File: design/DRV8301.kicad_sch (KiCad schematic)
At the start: 38 parts, among them U2 LM3671, U3 DRV8301

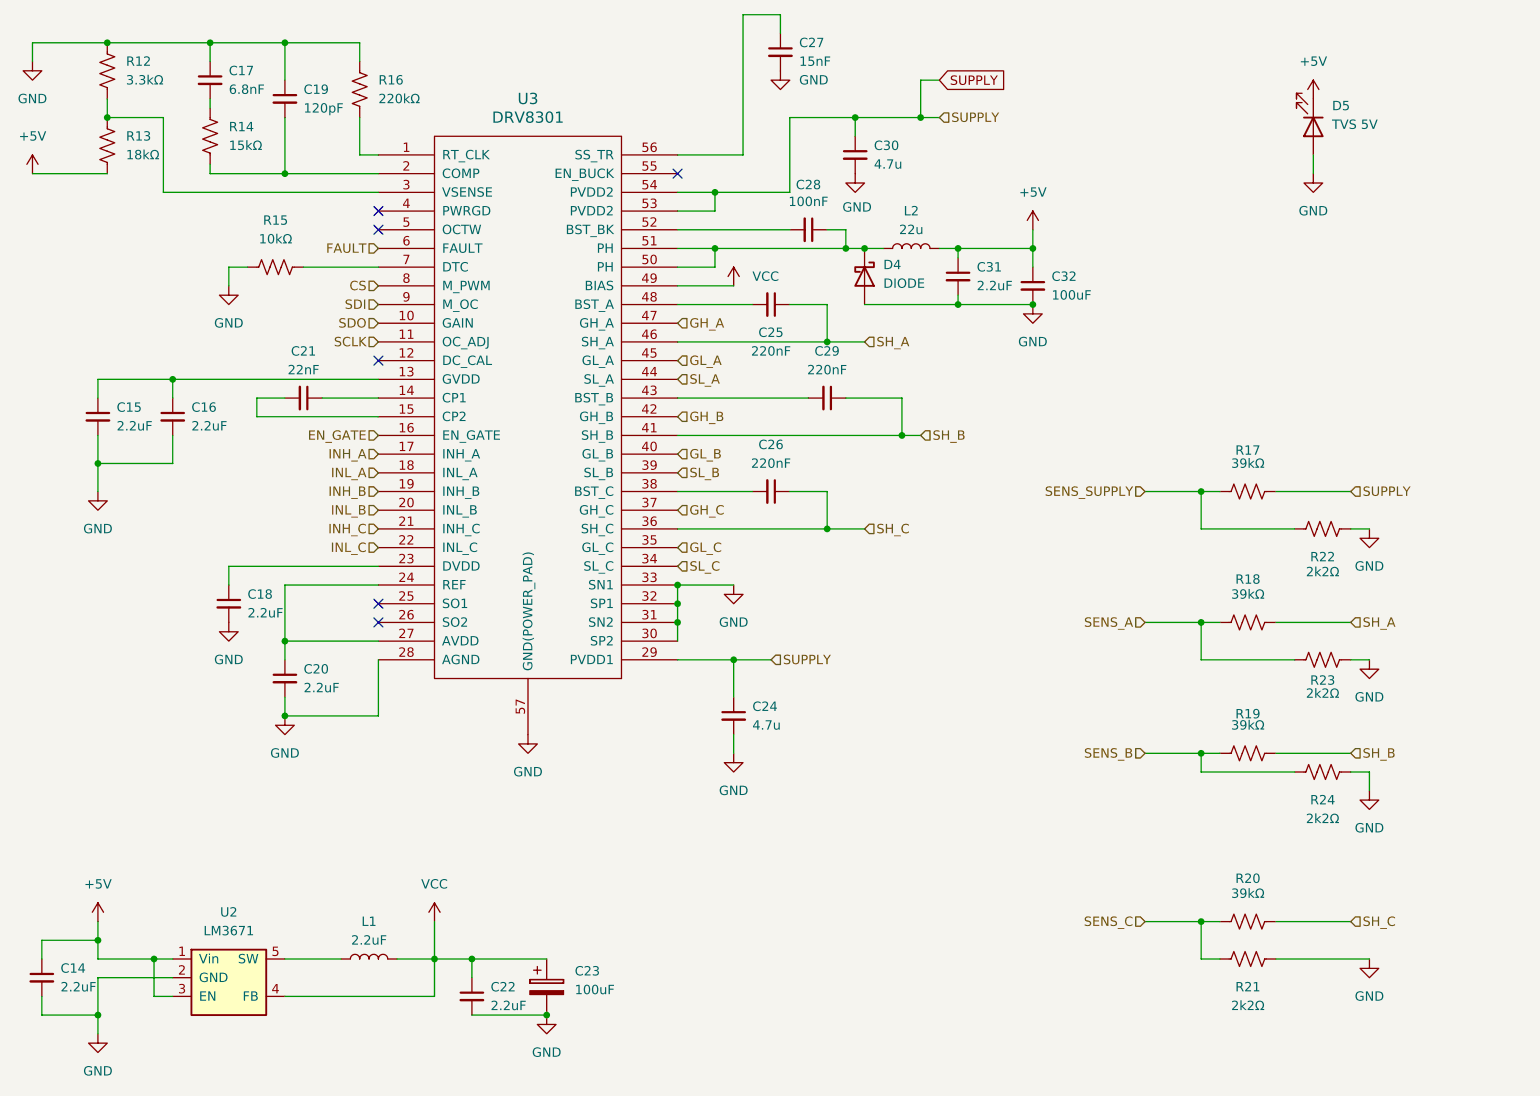
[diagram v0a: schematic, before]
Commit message: Agregado ibom
Pequeños cambios en el esquemático y agregado de ibom
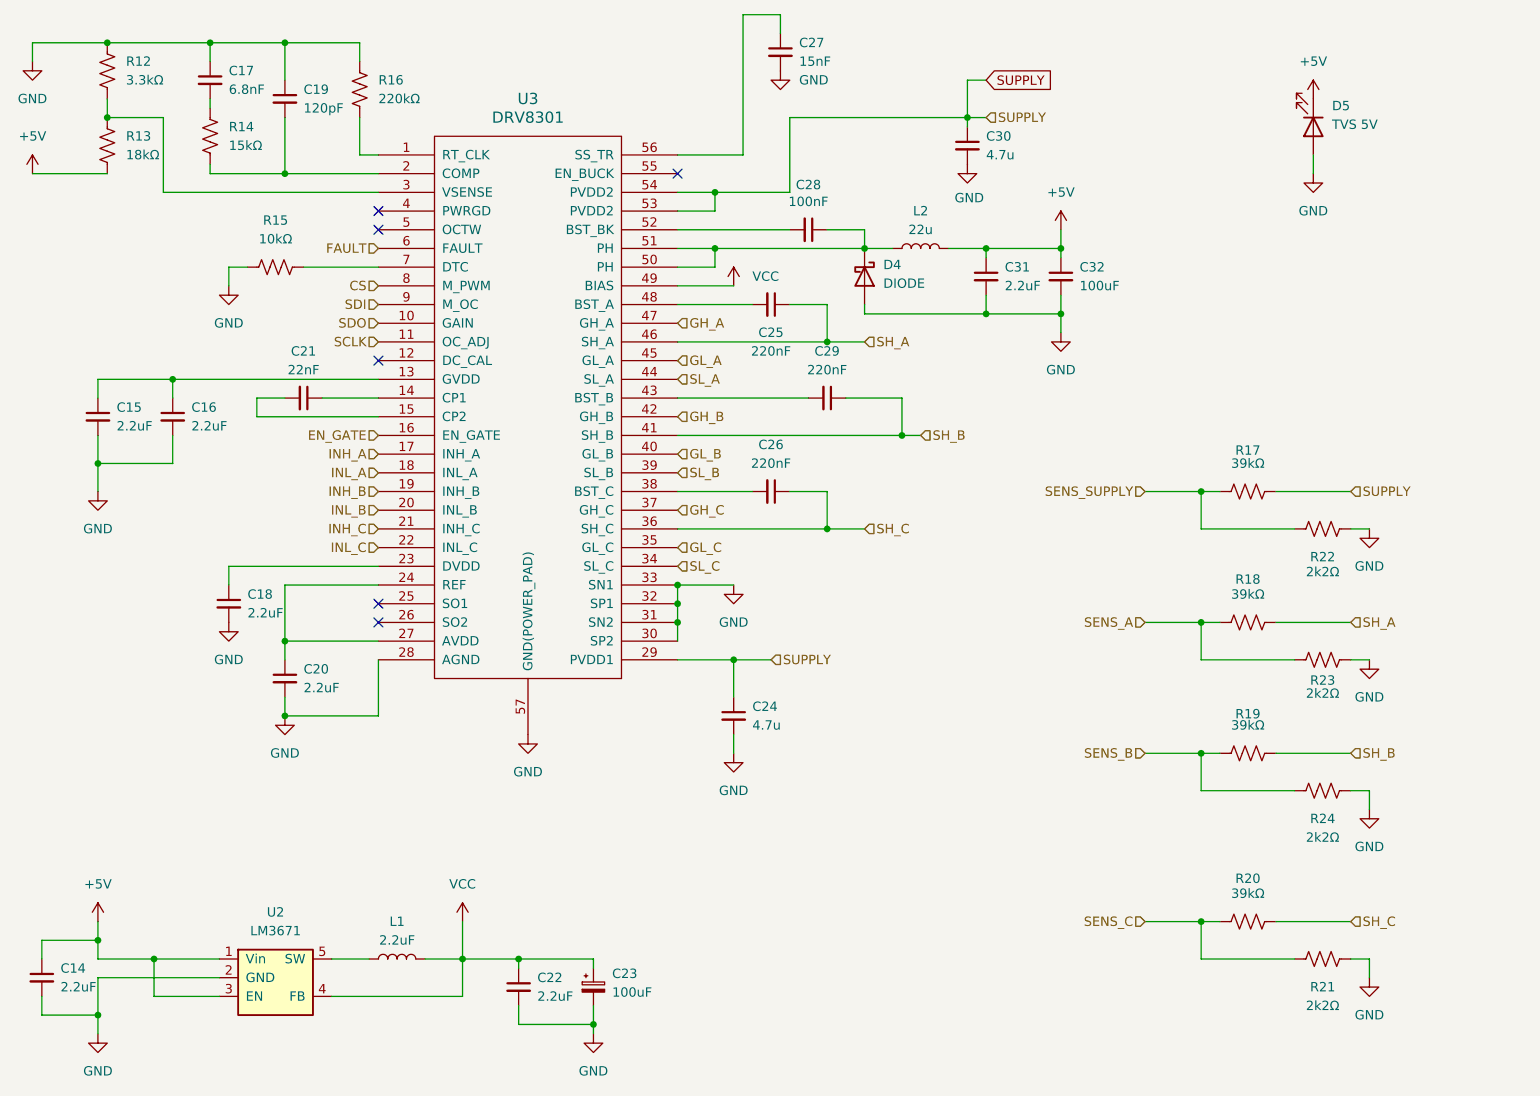
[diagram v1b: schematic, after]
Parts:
- C23: symbol ESCX-rescue:CP-Device -> Device:C_Polarized_Small
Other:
- moved on the sheet: C22, C30, C31, C32, L1, L2, R21, R24, U2

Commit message: Cambios en el esquemático
- Cambio de Vcc por +3.3V
- Agregado de hoja para desarrollar la entrada de tensión alterna
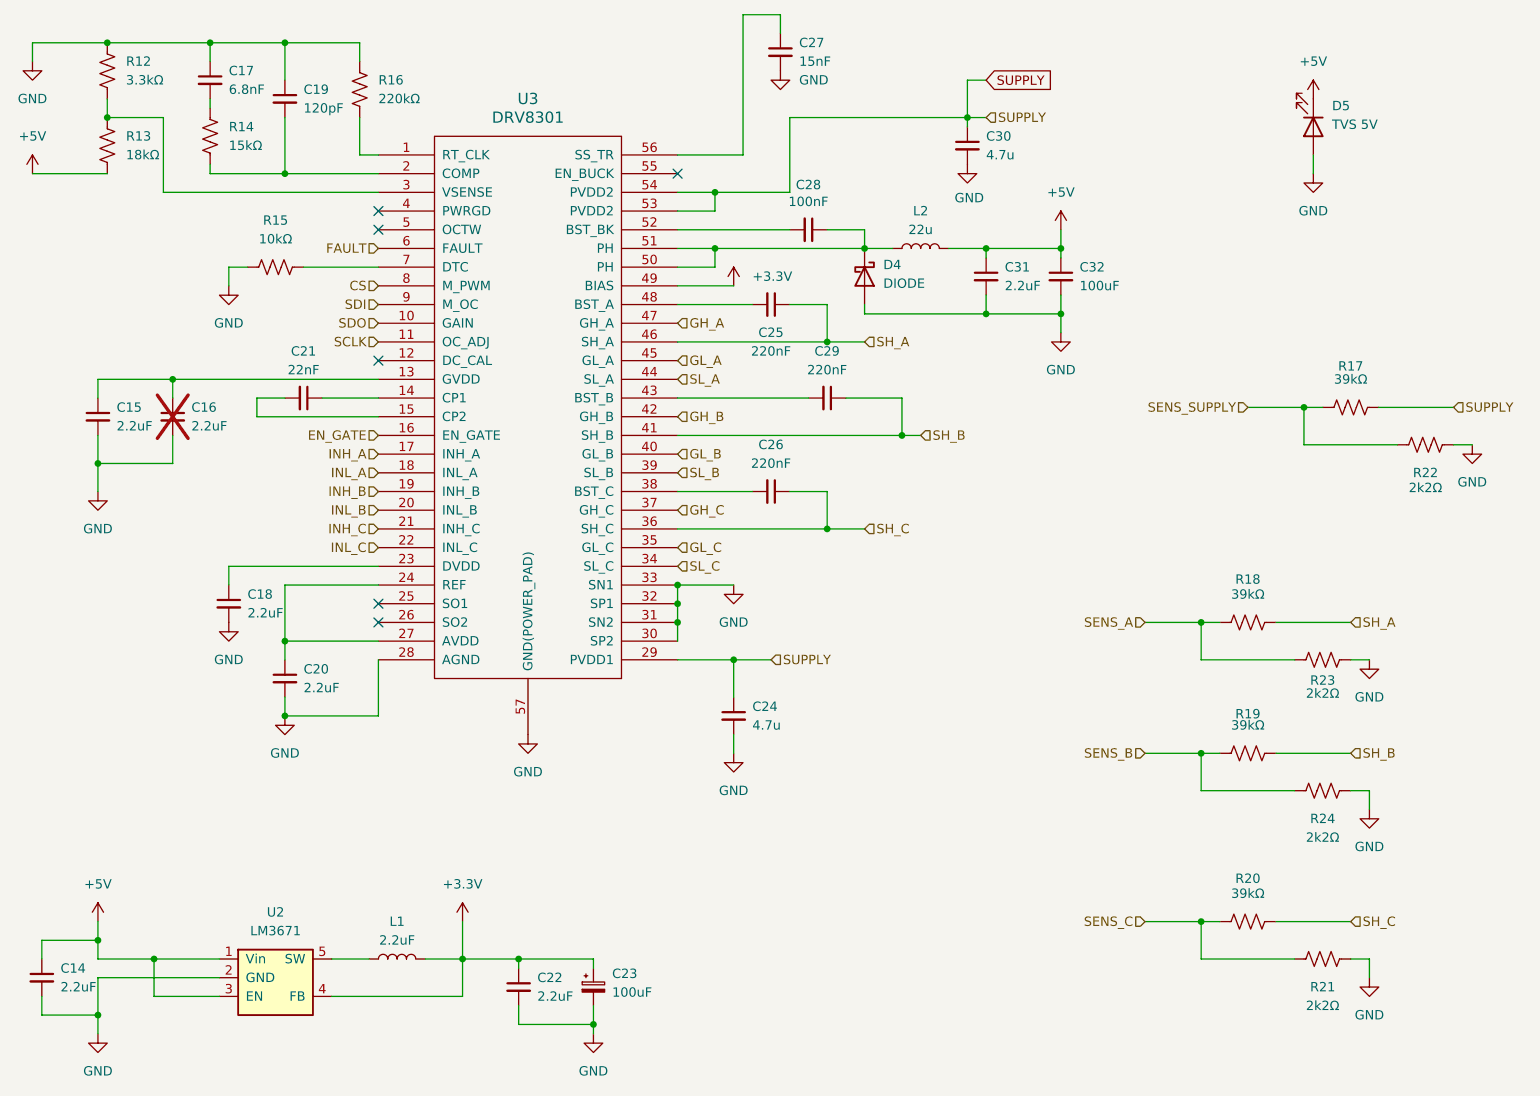
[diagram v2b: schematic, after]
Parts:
- C16: now not fitted; now left out of the parts list
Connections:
- net VCC renamed +3.3V
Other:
- moved on the sheet: R17, R22
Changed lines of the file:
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@@
 	)
 	(junction
-		(at 233.68 83.82)
+		(at 247.65 72.39)
 		(diameter 0)
 		(color 0 0 0 0)
@@
 	(wire
 		(pts
-			(xy 233.68 88.9) (xy 233.68 83.82)
+			(xy 247.65 77.47) (xy 247.65 72.39)
 		)
 		(stroke
@@
 	(wire
 		(pts
-			(xy 254 88.9) (xy 256.54 88.9)
+			(xy 267.97 77.47) (xy 270.51 77.47)
 		)
 		(stroke
@@
 	(wire
 		(pts
-			(xy 246.38 88.9) (xy 233.68 88.9)
+			(xy 260.35 77.47) (xy 247.65 77.47)
 		)
 		(stroke
@@
 	(wire
 		(pts
-			(xy 233.68 83.82) (xy 236.22 83.82)
+			(xy 247.65 72.39) (xy 250.19 72.39)
 		)
 		(stroke
@@
 	(wire
 		(pts
-			(xy 226.06 83.82) (xy 233.68 83.82)
+			(xy 240.03 72.39) (xy 247.65 72.39)
 		)
 		(stroke
@@
 	(wire
 		(pts
-			(xy 243.84 83.82) (xy 254 83.82)
+			(xy 257.81 72.39) (xy 267.97 72.39)
 		)
 		(stroke
@@
 	(hierarchical_label "SENS_SUPPLY"
 		(shape input)
-		(at 226.06 83.82 180)
+		(at 240.03 72.39 180)
 		(fields_autoplaced yes)
 		(effects
@@
 	(hierarchical_label "SUPPLY"
 		(shape input)
-		(at 254 83.82 0)
+		(at 267.97 72.39 0)
 		(fields_autoplaced yes)
 		(effects
@@
 		(at 93.98 73.66 0)
 		(unit 1)
-		(exclude_from_sim no)
-		(in_bom yes)
-		(on_board yes)
-		(dnp no)
+		(exclude_from_sim yes)
+		(in_bom no)
+		(on_board no)
+		(dnp yes)
 		(fields_autoplaced yes)
 		(property "Reference" "C16"
@@
 			)
 		)
-		(property "Value" "VCC"
+		(property "Value" "+3.3V"
 			(at 172.72 54.6099 0)
 			(effects
@@
 	(symbol
 		(lib_id "Device:R_US")
-		(at 240.03 83.82 270)
+		(at 254 72.39 270)
 		(unit 1)
 		(exclude_from_sim no)
@@
 		(dnp no)
 		(property "Reference" "R17"
-			(at 240.03 78.232 90)
+			(at 254 66.802 90)
 			(effects
 				(font
@@
 		)
 		(property "Value" "39kΩ"
-			(at 240.03 80.01 90)
+			(at 254 68.58 90)
 			(effects
 				(font
@@
 		)
 		(property "Footprint" "Resistor_SMD:R_0603_1608Metric"
-			(at 239.776 84.836 90)
+			(at 253.746 73.406 90)
 			(effects
 				(font
@@
 		)
 		(property "Datasheet" "~"
-			(at 240.03 83.82 0)
+			(at 254 72.39 0)
 			(effects
 				(font
@@
 		)
 		(property "Description" ""
-			(at 240.03 83.82 0)
+			(at 254 72.39 0)
 			(effects
 				(font
@@
 	(symbol
 		(lib_id "Device:R_US")
-		(at 250.19 88.9 270)
+		(at 264.16 77.47 270)
 		(unit 1)
 		(exclude_from_sim no)
@@
 		(dnp no)
 		(property "Reference" "R22"
-			(at 250.19 92.71 90)
+			(at 264.16 81.28 90)
 			(effects
 				(font
@@
 		)
 		(property "Value" "2k2Ω"
-			(at 250.19 94.742 90)
+			(at 264.16 83.312 90)
 			(effects
 				(font
@@
 		)
 		(property "Footprint" "Resistor_SMD:R_0603_1608Metric"
-			(at 249.936 89.916 90)
+			(at 263.906 78.486 90)
 			(effects
 				(font
@@
 		)
 		(property "Datasheet" "~"
-			(at 250.19 88.9 0)
+			(at 264.16 77.47 0)
 			(effects
 				(font
@@
 		)
 		(property "Description" "R 2k2, 0603 "
-			(at 250.19 88.9 0)
+			(at 264.16 77.47 0)
 			(effects
 				(font
@@
 	(symbol
 		(lib_id "power:GND")
-		(at 256.54 88.9 0)
+		(at 270.51 77.47 0)
 		(unit 1)
 		(exclude_from_sim no)
@@
 		(fields_autoplaced yes)
 		(property "Reference" "#PWR053"
-			(at 256.54 95.25 0)
+			(at 270.51 83.82 0)
 			(effects
 				(font
@@
 		)
 		(property "Value" "GND"
-			(at 256.54 93.98 0)
+			(at 270.51 82.55 0)
 			(effects
 				(font
@@
 		)
 		(property "Footprint" ""
-			(at 256.54 88.9 0)
+			(at 270.51 77.47 0)
 			(effects
 				(font
@@
 		)
 		(property "Datasheet" ""
-			(at 256.54 88.9 0)
+			(at 270.51 77.47 0)
 			(effects
 				(font
@@
 		)
 		(property "Description" "Power symbol creates a global label with name \"GND\" , ground"
-			(at 256.54 88.9 0)
+			(at 270.51 77.47 0)
 			(effects
 				(font
@@
 			)
 		)
-		(property "Value" "VCC"
+		(property "Value" "+3.3V"
 			(at 133.35 137.16 0)
 			(effects
@@
 			)
 		)
-		(property "Datasheet" ""
+		(property "Datasheet" "https://www.ti.com/product/es-mx/DRV8301"
 			(at 142.24 72.39 0)
 			(effects
@@
 					(size 1.524 1.524)
 				)
+				(hide yes)
 			)
 		)

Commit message: Commit antes del merge
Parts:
- removed R17, R18, R19, R20: 39kΩ, Resistor_SMD:R_0603_1608Metric, symbol Device:R_US
- removed R21, R22, R23, R24: 2k2Ω, Resistor_SMD:R_0603_1608Metric, symbol Device:R_US
